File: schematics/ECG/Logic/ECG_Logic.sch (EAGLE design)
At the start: 72 parts, among them IC1 ADS1293, IC2 LIS3DH, IC3 MCP1703, IC4 CC2541, IC5 FSA4157, IC6 FSA4157, IC7 FSA4157, IC8 BALUN_2450BM_SERIES_SMD, X1 XTAL-2SMD, X2 XTAL_403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

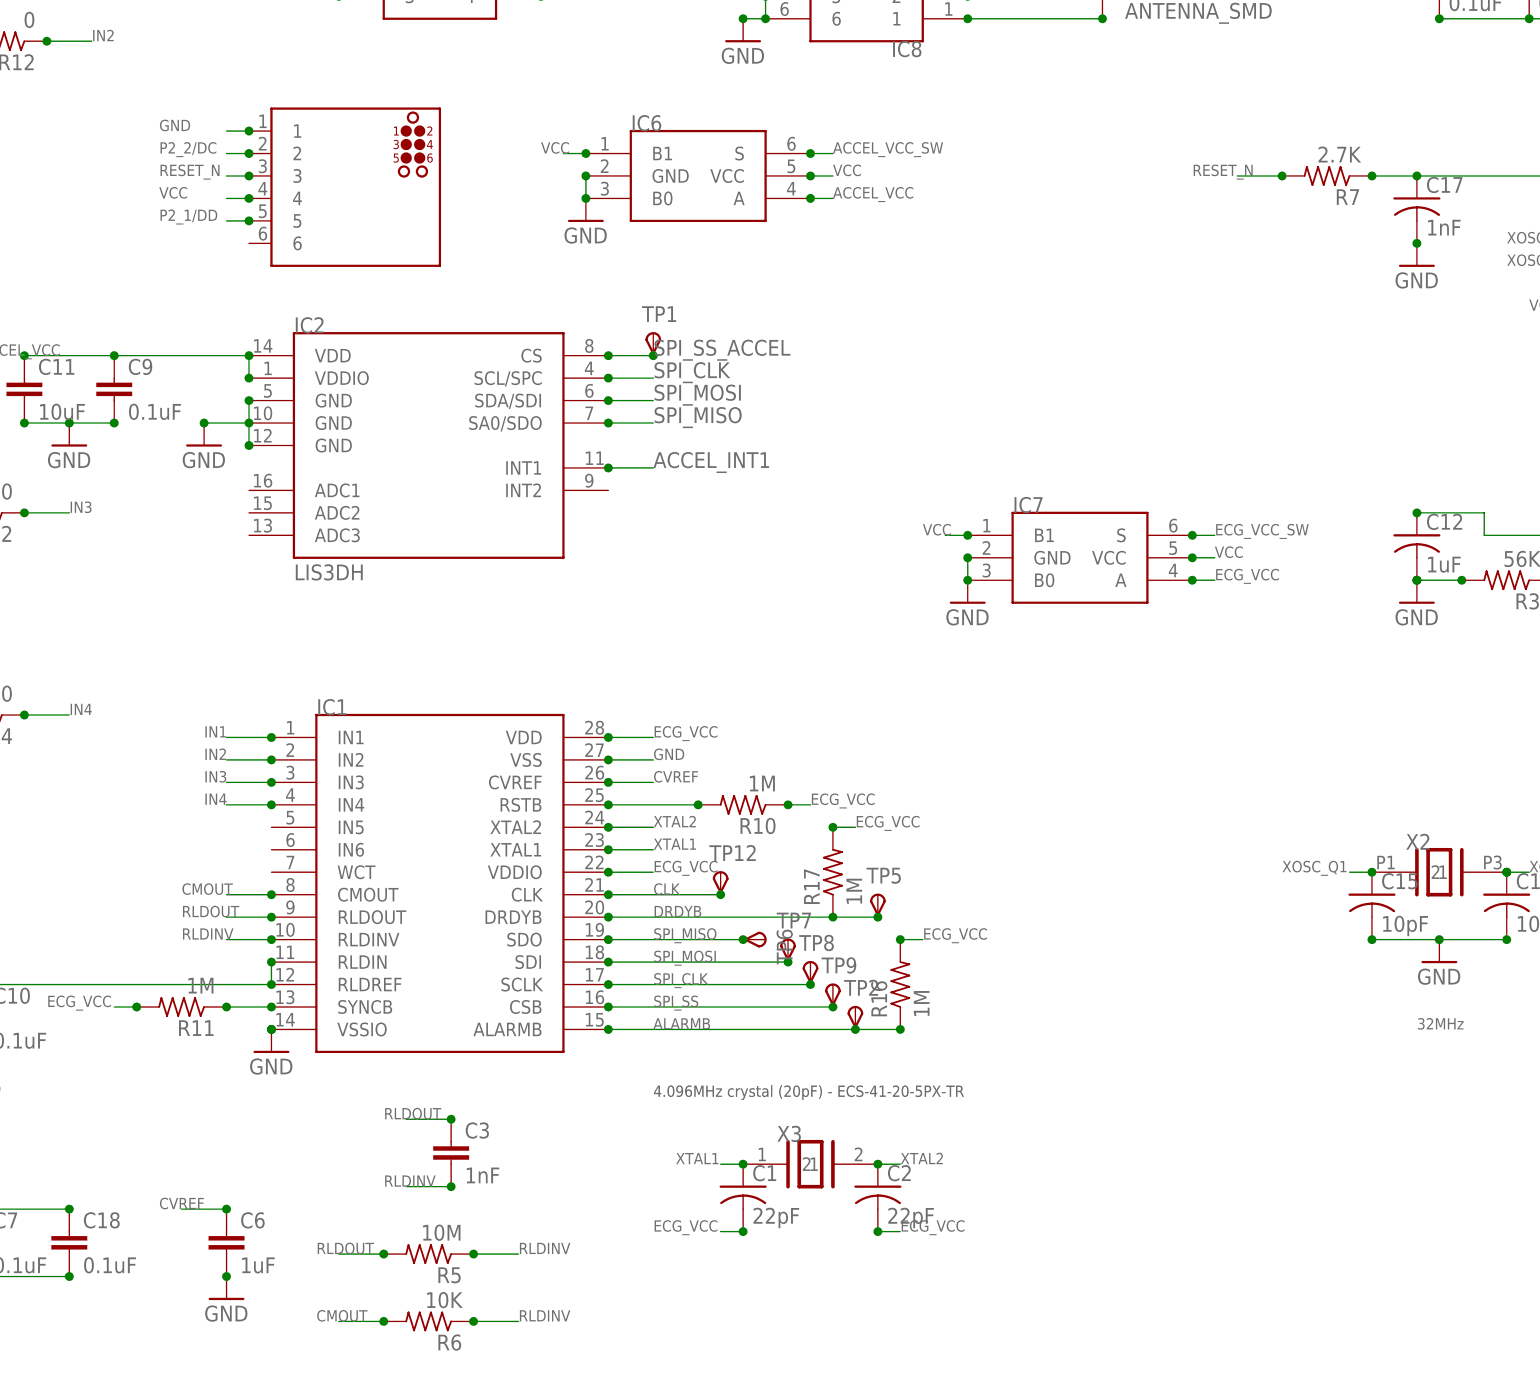
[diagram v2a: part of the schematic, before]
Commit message: replaced ADS1293 crystal with LTC6907. Fixed 6 pin programming header wiring
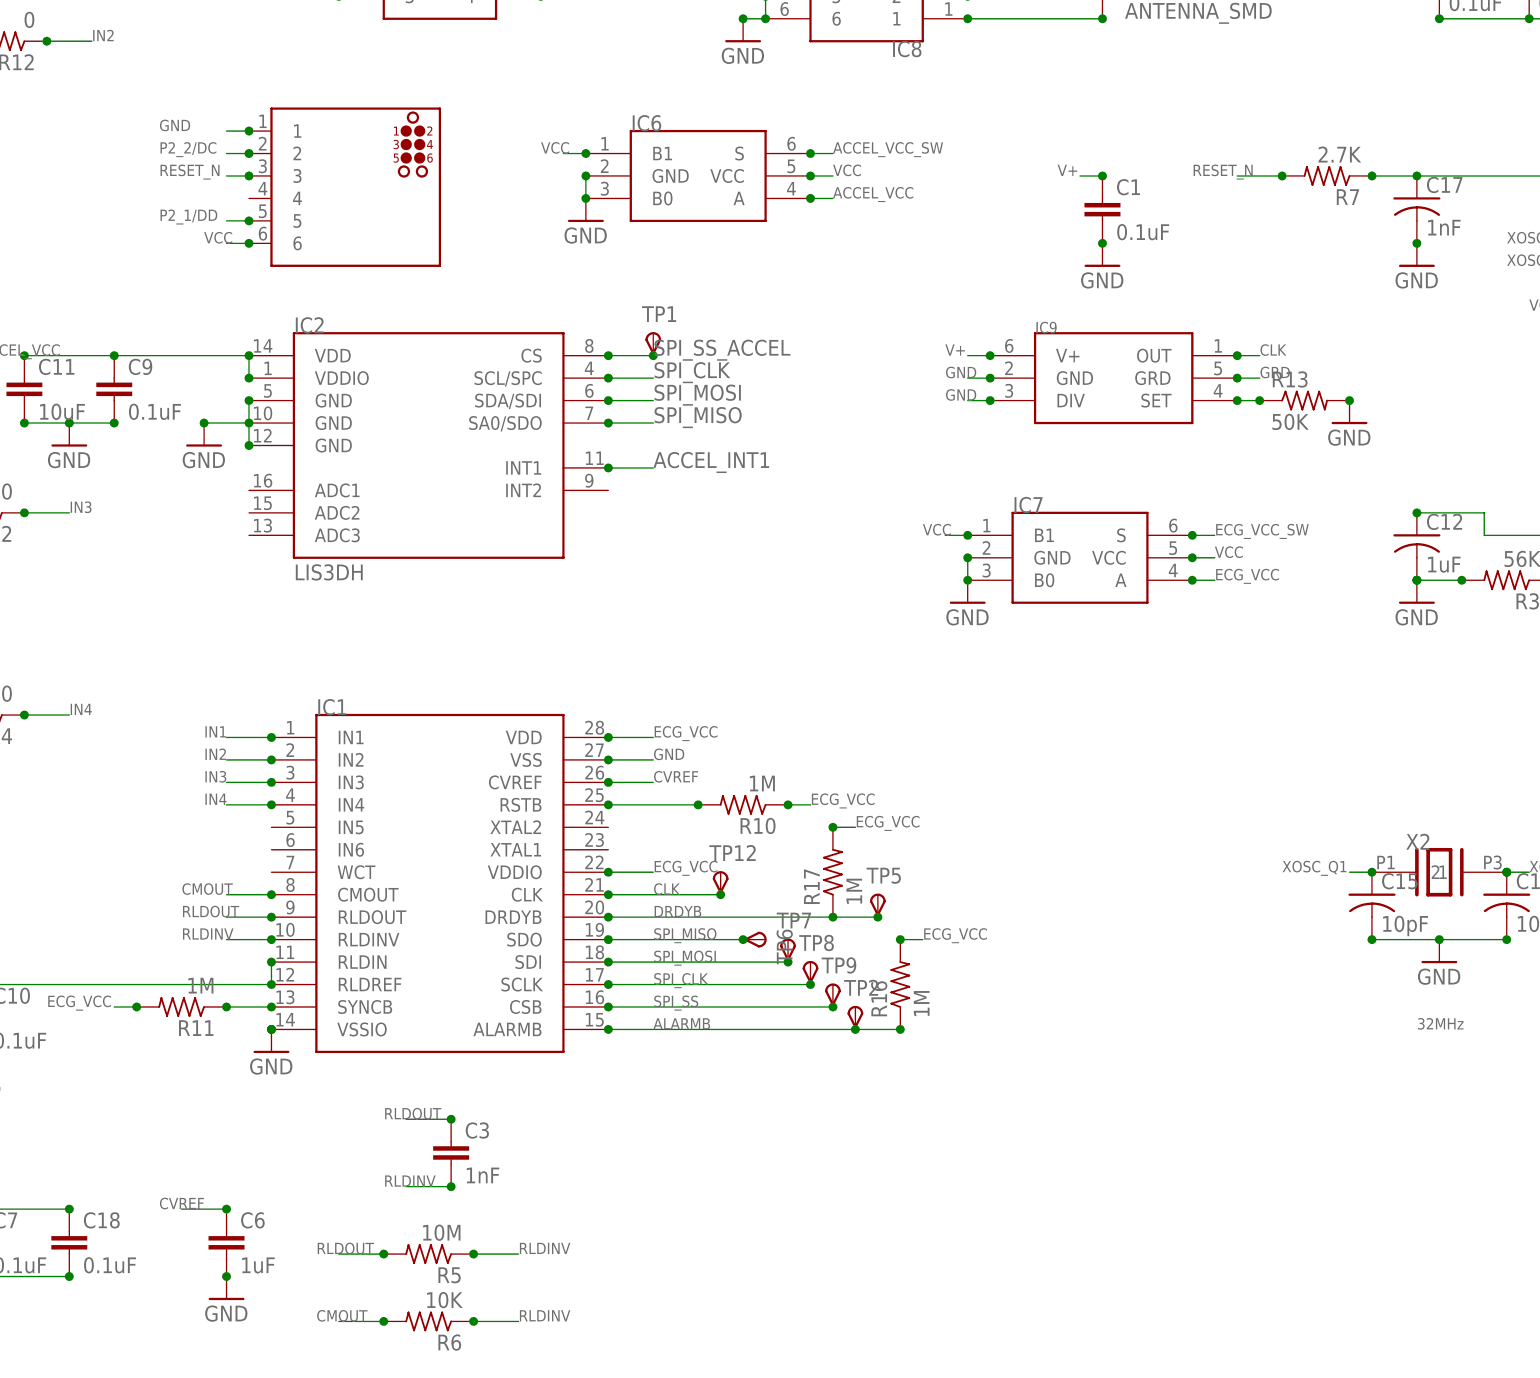
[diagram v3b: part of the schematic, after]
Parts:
- removed C2: 22pF, rcl:C-USC0201
- removed X3: XTAL-CSM7, ecs:XTAL-CSM7
- added IC9: LTC6907, linear:LTC6907
- added R13: 50K, rcl:R-US_R0603
- C1: value 22pF -> 0.1uF; device rcl:C-USC0201 -> rcl:C-EUC0201
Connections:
- removed net XTAL1: C1.1, IC1.XTAL1, X3.1
- removed net XTAL2: C2.1, IC1.XTAL2, X3.2
- new net GRD: IC9.GRD
- new net N$14: IC9.SET, R13.1
- new net V+: C1.1, IC9.V+
- net CLK: now also IC9.OUT
- net ECG_VCC: no longer C1.2, C2.2
- net GND: now also C1.2, IC9.DIV, IC9.GND, R13.2
- net VCC: now also PROG.6; no longer PROG.4
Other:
- note removed: "4.096MHz crystal (20pF) - ECS-41-20-5PX-TR"
- moved on the sheet: C1
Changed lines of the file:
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@@
 <?xml version="1.0" encoding="utf-8"?>
 <!DOCTYPE eagle SYSTEM "eagle.dtd">
-<eagle version="6.4">
+<eagle version="6.5.0">
 <drawing>
 <settings>
@@
 <parts>
 <part name="IC1" library="texas_instruments" deviceset="ADS1293" device=""/>
-<part name="C2" library="rcl" deviceset="C-US" device="C0201" value="22pF"/>
-<part name="X3" library="ecs" deviceset="XTAL-CSM7" device=""/>
 <part name="CONN1" library="harwin" deviceset="10POS_1.27MM_SMD" device=""/>
-<part name="C1" library="rcl" deviceset="C-US" device="C0201" value="22pF"/>
 <part name="C3" library="rcl" deviceset="C-EU" device="C0201" value="1nF"/>
 <part name="C6" library="rcl" deviceset="C-EU" device="C0201" value="1uF"/>
@@
 <part name="TP1" library="testpad" deviceset="TPS" device="TP08SQ"/>
 <part name="TP2" library="testpad" deviceset="TPS" device="TP06R" value="TPSTP06R"/>
+<part name="IC9" library="linear" deviceset="LTC6907" device=""/>
+<part name="C1" library="rcl" deviceset="C-EU" device="C0201" value="0.1uF"/>
+<part name="GND25" library="supply1" deviceset="GND" device=""/>
+<part name="R13" library="rcl" deviceset="R-US_" device="R0603" value="50K"/>
+<part name="GND26" library="supply1" deviceset="GND" device=""/>
 </parts>
 <sheets>
 <sheet>
 <plain>
-<text x="96.52" y="33.02" size="1.27" layer="97">4.096MHz crystal (20pF) - ECS-41-20-5PX-TR</text>
 <text x="182.88" y="40.64" size="1.27" layer="95">32MHz</text>
 <text x="236.22" y="40.64" size="1.27" layer="95">32.768KHz</text>
@@
 <instances>
 <instance part="IC1" gate="IC" x="71.12" y="58.42"/>
-<instance part="C2" gate="G$1" x="121.92" y="22.86"/>
-<instance part="X3" gate="XTAL" x="114.3" y="25.4"/>
 <instance part="CONN1" gate="CONN" x="30.48" y="198.12"/>
-<instance part="C1" gate="G$1" x="106.68" y="22.86"/>
 <instance part="C3" gate="G$1" x="73.66" y="27.94"/>
 <instance part="C6" gate="G$1" x="48.26" y="17.78"/>
@@
 <instance part="TP1" gate="G$1" x="96.52" y="119.38"/>
 <instance part="TP2" gate="G$1" x="119.38" y="43.18"/>
+<instance part="IC9" gate="IC" x="147.32" y="114.3"/>
+<instance part="C1" gate="G$1" x="147.32" y="134.62"/>
+<instance part="GND25" gate="1" x="147.32" y="127"/>
+<instance part="R13" gate="G$1" x="170.18" y="111.76"/>
+<instance part="GND26" gate="1" x="175.26" y="109.22"/>
 </instances>
 <busses>
@@
 <junction x="50.8" y="142.24"/>
 <label x="40.64" y="142.24" size="1.27" layer="95"/>
+</segment>
+<segment>
+<pinref part="GND25" gate="1" pin="GND"/>
+<pinref part="C1" gate="G$1" pin="2"/>
+<junction x="147.32" y="129.54"/>
+</segment>
+<segment>
+<pinref part="IC9" gate="IC" pin="GND"/>
+<wire x1="134.62" y1="114.3" x2="132.08" y2="114.3" width="0.1524" layer="91"/>
+<junction x="134.62" y="114.3"/>
+<label x="129.54" y="114.3" size="1.27" layer="95"/>
+</segment>
+<segment>
+<pinref part="IC9" gate="IC" pin="DIV"/>
+<wire x1="134.62" y1="111.76" x2="132.08" y2="111.76" width="0.1524" layer="91"/>
+<junction x="134.62" y="111.76"/>
+<label x="129.54" y="111.76" size="1.27" layer="95"/>
+</segment>
+<segment>
+<pinref part="R13" gate="G$1" pin="2"/>
+<pinref part="GND26" gate="1" pin="GND"/>
+<junction x="175.26" y="111.76"/>
 </segment>
 </net>
@@
 </segment>
 <segment>
-<pinref part="PROG" gate="G$1" pin="4"/>
-<wire x1="50.8" y1="134.62" x2="48.26" y2="134.62" width="0.1524" layer="91"/>
-<junction x="50.8" y="134.62"/>
-<label x="40.64" y="134.62" size="1.27" layer="95"/>
+<pinref part="PROG" gate="G$1" pin="6"/>
+<wire x1="50.8" y1="129.54" x2="48.26" y2="129.54" width="0.1524" layer="91"/>
+<junction x="50.8" y="129.54"/>
+<label x="45.72" y="129.54" size="1.27" layer="95"/>
 </segment>
 </net>
@@
 <pinref part="IC8" gate="IC" pin="4"/>
 <label x="101.6" y="160.02" size="1.27" layer="95"/>
-</segment>
-</net>
-<net name="XTAL2" class="0">
-<segment>
-<pinref part="IC1" gate="IC" pin="XTAL2"/>
-<wire x1="91.44" y1="63.5" x2="96.52" y2="63.5" width="0.1524" layer="91"/>
-<junction x="91.44" y="63.5"/>
-<label x="96.52" y="63.5" size="1.27" layer="95"/>
-</segment>
-<segment>
-<pinref part="X3" gate="XTAL" pin="2"/>
-<pinref part="C2" gate="G$1" pin="1"/>
-<junction x="121.92" y="25.4"/>
-<wire x1="121.92" y1="25.4" x2="124.46" y2="25.4" width="0.1524" layer="91"/>
-<label x="124.46" y="25.4" size="1.27" layer="95"/>
-</segment>
-</net>
-<net name="XTAL1" class="0">
-<segment>
-<pinref part="IC1" gate="IC" pin="XTAL1"/>
-<wire x1="91.44" y1="60.96" x2="96.52" y2="60.96" width="0.1524" layer="91"/>
-<junction x="91.44" y="60.96"/>
-<label x="96.52" y="60.96" size="1.27" layer="95"/>
-</segment>
-<segment>
-<pinref part="X3" gate="XTAL" pin="1"/>
-<pinref part="C1" gate="G$1" pin="1"/>
-<wire x1="106.68" y1="25.4" x2="104.14" y2="25.4" width="0.1524" layer="91"/>
-<junction x="106.68" y="25.4"/>
-<label x="99.06" y="25.4" size="1.27" layer="95"/>
 </segment>
 </net>
@@
 <label x="96.52" y="55.88" size="1.27" layer="95"/>
 </segment>
+<segment>
+<pinref part="IC9" gate="IC" pin="OUT"/>
+<wire x1="162.56" y1="116.84" x2="165.1" y2="116.84" width="0.1524" layer="91"/>
+<junction x="162.56" y="116.84"/>
+<label x="165.1" y="116.84" size="1.27" layer="95"/>
+</segment>
 </net>
 <net name="ECG_VCC_SW" class="0">
@@
 </segment>
 <segment>
-<wire x1="104.14" y1="17.78" x2="106.68" y2="17.78" width="0.1524" layer="91"/>
-<pinref part="C1" gate="G$1" pin="2"/>
-<junction x="106.68" y="17.78"/>
-<label x="96.52" y="17.78" size="1.27" layer="95"/>
-</segment>
-<segment>
-<wire x1="124.46" y1="17.78" x2="121.92" y2="17.78" width="0.1524" layer="91"/>
-<pinref part="C2" gate="G$1" pin="2"/>
-<junction x="121.92" y="17.78"/>
-<label x="124.46" y="17.78" size="1.27" layer="95"/>
-</segment>
-<segment>
 <pinref part="R10" gate="G$1" pin="1"/>
 <wire x1="111.76" y1="66.04" x2="114.3" y2="66.04" width="0.1524" layer="91"/>
@@
 </segment>
 </net>
+<net name="N$14" class="0">
+<segment>
+<pinref part="IC9" gate="IC" pin="SET"/>
+<wire x1="162.56" y1="111.76" x2="165.1" y2="111.76" width="0.1524" layer="91"/>
+<pinref part="R13" gate="G$1" pin="1"/>
+<junction x="165.1" y="111.76"/>
+<junction x="162.56" y="111.76"/>
+</segment>
+</net>
+<net name="V+" class="0">
+<segment>
+<pinref part="C1" gate="G$1" pin="1"/>
+<wire x1="147.32" y1="137.16" x2="144.78" y2="137.16" width="0.1524" layer="91"/>
+<junction x="147.32" y="137.16"/>
+<label x="142.24" y="137.16" size="1.27" layer="95"/>
+</segment>
+<segment>
+<pinref part="IC9" gate="IC" pin="V+"/>
+<wire x1="134.62" y1="116.84" x2="132.08" y2="116.84" width="0.1524" layer="91"/>
+<junction x="134.62" y="116.84"/>
+<label x="129.54" y="116.84" size="1.27" layer="95"/>
+</segment>
+</net>
+<net name="GRD" class="0">
+<segment>
+<pinref part="IC9" gate="IC" pin="GRD"/>
+<junction x="162.56" y="114.3"/>
+<wire x1="162.56" y1="114.3" x2="165.1" y2="114.3" width="0.1524" layer="91"/>
+<label x="165.1" y="114.3" size="1.27" layer="95"/>
+</segment>
+</net>

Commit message: replaced vertical headers with right angle spring loaded headers. routed osc power to pin2 of cc2541
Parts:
- removed CONN2: M80-4V, harwin:M80-4V
- removed CONN3: M80-6V, harwin:M80-6V
- added U$1, U$2, U$3, U$4, U$5, U$6: TARGET_RA, pins:TARGET_RA
- TP12: value TPSTP06R -> TPSTP11R; device testpad:TPSTP06R -> testpad:TPSTP11R
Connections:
- removed net V+: C1.1, IC9.V+
- new net ADS1923_OSC_VCC: C1.1, IC4.SCL, IC9.V+
- net BATT: now also U$6.1; no longer CONN2.1
- net GND: now also U$5.1; no longer CONN2.2
- net LA: now also U$2.1; no longer CONN3.1
- net LL: now also U$1.1; no longer CONN3.6
- net RA: now also U$3.1; no longer CONN3.3
- net RL: now also U$4.1; no longer CONN3.4

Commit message: added analog switch to OSC. OSC resistor changed to 500K ohm for 400KHz operation
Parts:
- added IC10: FSA4157, fairchild:FSA4157
- R13: value 50K -> 500K; device rcl:R-US_R0603 -> rcl:R-US_R1206
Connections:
- removed net ADS1293_RESET: IC4.P1_3
- removed net ADS1923_OSC_VCC: C1.1, IC4.SCL, IC9.V+
- new net OSC_SW_VCC: IC10.S, IC4.SCL
- new net OSC_VCC: C1.1, IC10.A, IC9.V+
- net GND: now also IC10.B0, IC10.GND
- net VCC: now also IC10.B1, IC10.VCC
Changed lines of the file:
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@@
 <?xml version="1.0" encoding="utf-8"?>
 <!DOCTYPE eagle SYSTEM "eagle.dtd">
-<eagle version="6.5.0">
+<eagle version="6.4">
 <drawing>
 <settings>
@@
 <part name="C1" library="rcl" deviceset="C-EU" device="C0201" value="0.1uF"/>
 <part name="GND25" library="supply1" deviceset="GND" device=""/>
-<part name="R13" library="rcl" deviceset="R-US_" device="R0603" value="50K"/>
+<part name="R13" library="rcl" deviceset="R-US_" device="R1206" value="500K"/>
 <part name="GND26" library="supply1" deviceset="GND" device=""/>
 <part name="U$1" library="pins" deviceset="TARGET_RA" device=""/>
@@
 <part name="U$5" library="pins" deviceset="TARGET_RA" device=""/>
 <part name="U$6" library="pins" deviceset="TARGET_RA" device=""/>
+<part name="IC10" library="fairchild" deviceset="FSA4157" device=""/>
+<part name="GND17" library="supply1" deviceset="GND" device=""/>
 </parts>
 <sheets>
@@
 <instance part="U$5" gate="PIN" x="187.96" y="195.58"/>
 <instance part="U$6" gate="PIN" x="187.96" y="193.04"/>
+<instance part="IC10" gate="FSA4157" x="68.58" y="162.56"/>
+<instance part="GND17" gate="1" x="55.88" y="157.48"/>
 </instances>
 <busses>
@@
 <junction x="182.88" y="195.58"/>
 <label x="175.26" y="195.58" size="1.27" layer="95"/>
+</segment>
+<segment>
+<pinref part="IC10" gate="FSA4157" pin="GND"/>
+<pinref part="IC10" gate="FSA4157" pin="B0"/>
+<wire x1="55.88" y1="162.56" x2="55.88" y2="160.02" width="0.1524" layer="91"/>
+<pinref part="GND17" gate="1" pin="GND"/>
+<junction x="55.88" y="160.02"/>
+<junction x="55.88" y="162.56"/>
 </segment>
 </net>
@@
 <label x="45.72" y="129.54" size="1.27" layer="95"/>
 </segment>
+<segment>
+<pinref part="IC10" gate="FSA4157" pin="VCC"/>
+<junction x="81.28" y="162.56"/>
+<wire x1="81.28" y1="162.56" x2="83.82" y2="162.56" width="0.1524" layer="91"/>
+<label x="83.82" y="162.56" size="1.27" layer="95"/>
+</segment>
+<segment>
+<pinref part="IC10" gate="FSA4157" pin="B1"/>
+<junction x="55.88" y="165.1"/>
+<wire x1="55.88" y1="165.1" x2="53.34" y2="165.1" width="0.1524" layer="91"/>
+<label x="50.8" y="165.1" size="1.27" layer="95"/>
+</segment>
 </net>
 <net name="RESET_N" class="0">
@@
 <junction x="101.6" y="200.66"/>
 <pinref part="R14" gate="G$1" pin="2"/>
-</segment>
-</net>
-<net name="ADS1293_RESET" class="0">
-<segment>
-<pinref part="IC4" gate="G$1" pin="P1_3"/>
-<wire x1="243.84" y1="109.22" x2="248.92" y2="109.22" width="0.1524" layer="91"/>
-<junction x="243.84" y="109.22"/>
-<label x="248.92" y="109.22" size="1.27" layer="95"/>
 </segment>
 </net>
@@
 </segment>
 </net>
-<net name="ADS1923_OSC_VCC" class="0">
+<net name="OSC_SW_VCC" class="0">
 <segment>
 <pinref part="IC4" gate="G$1" pin="SCL"/>
 <wire x1="205.74" y1="78.74" x2="203.2" y2="78.74" width="0.1524" layer="91"/>
 <junction x="205.74" y="78.74"/>
-<label x="187.96" y="78.74" size="1.27" layer="95"/>
+<label x="190.5" y="78.74" size="1.27" layer="95"/>
+</segment>
+<segment>
+<pinref part="IC10" gate="FSA4157" pin="S"/>
+<junction x="81.28" y="165.1"/>
+<wire x1="81.28" y1="165.1" x2="83.82" y2="165.1" width="0.1524" layer="91"/>
+<label x="83.82" y="165.1" size="1.27" layer="95"/>
+</segment>
+</net>
+<net name="OSC_VCC" class="0">
+<segment>
+<pinref part="C1" gate="G$1" pin="1"/>
+<wire x1="147.32" y1="137.16" x2="144.78" y2="137.16" width="0.1524" layer="91"/>
+<junction x="147.32" y="137.16"/>
+<label x="137.16" y="137.16" size="1.27" layer="95"/>
 </segment>
 <segment>
@@
 <wire x1="134.62" y1="116.84" x2="132.08" y2="116.84" width="0.1524" layer="91"/>
 <junction x="134.62" y="116.84"/>
-<label x="116.84" y="116.84" size="1.27" layer="95"/>
-</segment>
-<segment>
-<pinref part="C1" gate="G$1" pin="1"/>
-<wire x1="147.32" y1="137.16" x2="144.78" y2="137.16" width="0.1524" layer="91"/>
-<junction x="147.32" y="137.16"/>
-<label x="129.54" y="137.16" size="1.27" layer="95"/>
+<label x="124.46" y="116.84" size="1.27" layer="95"/>
+</segment>
+<segment>
+<pinref part="IC10" gate="FSA4157" pin="A"/>
+<junction x="81.28" y="160.02"/>
+<wire x1="81.28" y1="160.02" x2="83.82" y2="160.02" width="0.1524" layer="91"/>
+<label x="83.82" y="160.02" size="1.27" layer="95"/>
 </segment>
 </net>
@@
 </sheet>
 </sheets>
+<errors>
+</errors>
 </schematic>
 </drawing>
